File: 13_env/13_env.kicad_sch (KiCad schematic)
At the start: 51 parts, among them J1 gate in 1, J3 Eurorack, J5 env out 1, J6 End of Cycle Out, Q1 BC848, Q2 BC858, Q3 BC848, Q4 BC858, SW1 Manual Gate, SW2 Normal/Inverted, SW4 Gate/Loop, U1 TL074, U2 TL072

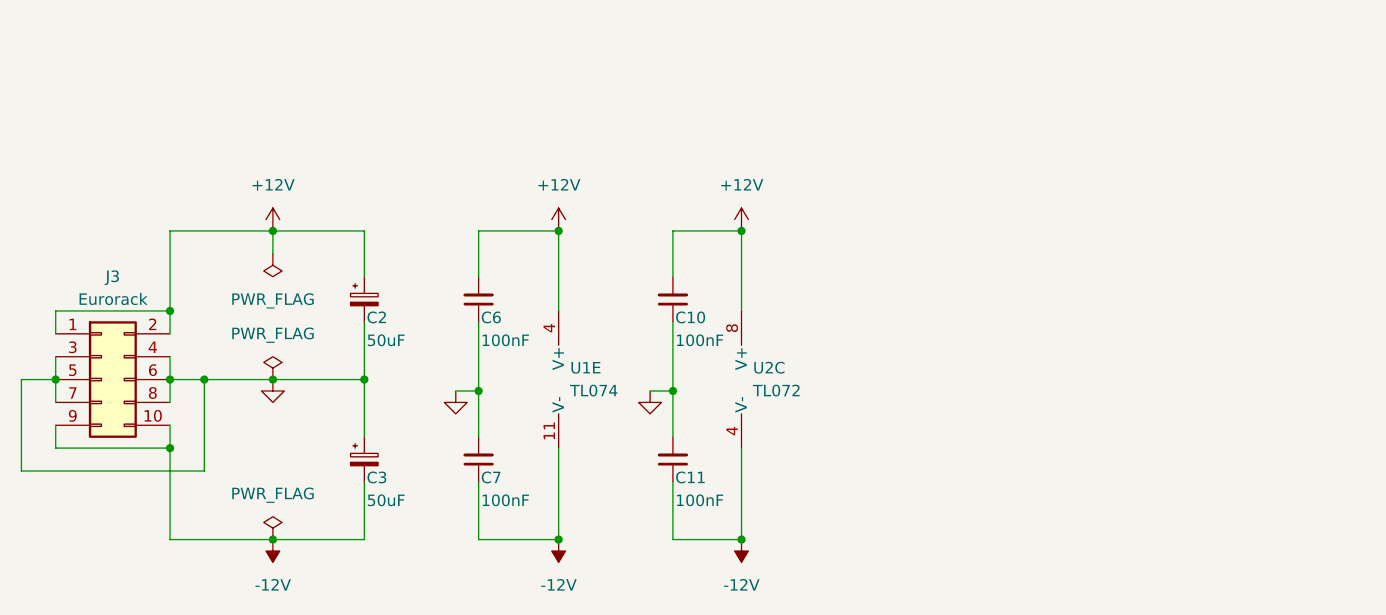
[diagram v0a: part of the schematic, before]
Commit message: added diodes
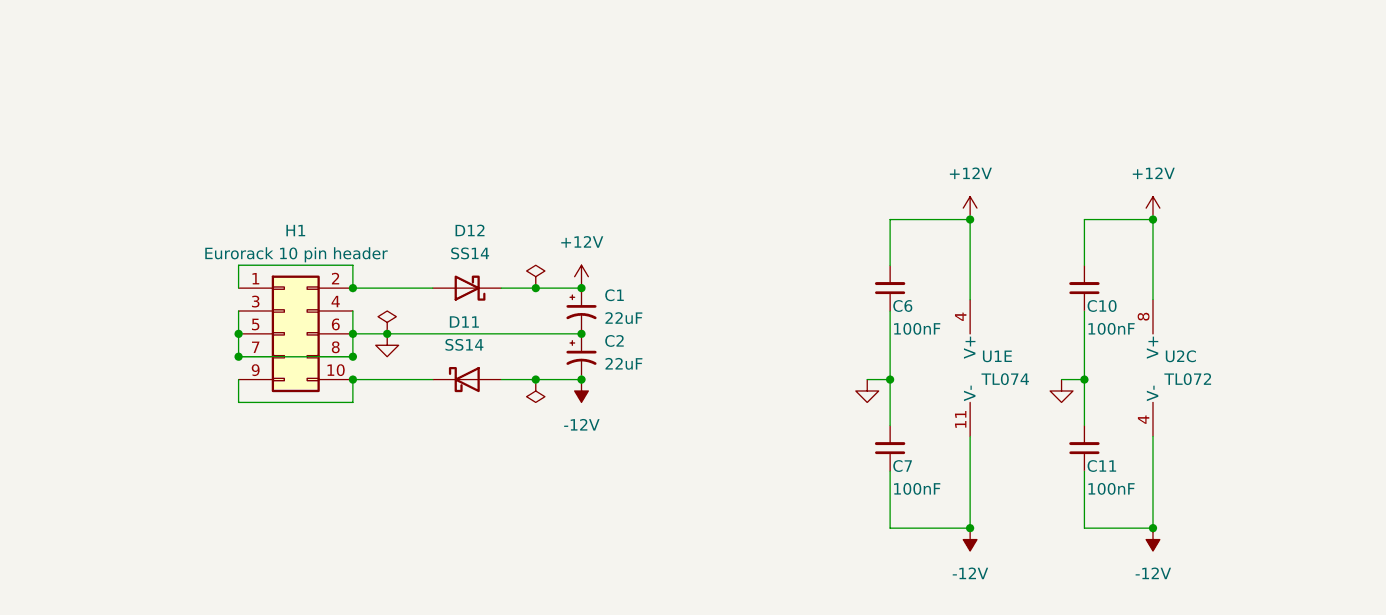
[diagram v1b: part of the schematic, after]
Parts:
- removed C2, C3: 50uF, Capacitor_THT:CP_Radial_D6.3mm_P2.50mm, symbol Device:C_Polarized_Small
- removed J3: Eurorack, cynthia:Eurorack Header, symbol Connector_Generic:Conn_02x05_Odd_Even
- added C1, C2: 22uF, Capacitor_THT:CP_Radial_D6.3mm_P2.50mm, symbol Device:C_Polarized_Small_US
- added D11, D12: SS14, Diode_SMD:D_SMA, symbol Diode:SS14
- added H1: Eurorack 10 pin header, cynthia:Eurorack Header, symbol Connector_Generic:Conn_02x05_Odd_Even
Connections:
- net +12V: now also C1.1, D12.1 (K)
- net -12V: now also C2.2, D11.2 (A)
- net GND: now also C1.2, C2.1, H1.3 (Pin_3), H1.4 (Pin_4), H1.5 (Pin_5), H1.6 (Pin_6), H1.7 (Pin_7), H1.8 (Pin_8)
- new net: D12.2 (A), H1.1 (Pin_1), H1.2 (Pin_2)
- new net: D11.1 (K), H1.10 (Pin_10), H1.9 (Pin_9)
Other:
- moved on the sheet: C10, C11, C6, C7, U1E, U2C

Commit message: updated 13 pcb
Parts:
- C10, C11, C6, C7, C8, C9: footprint Capacitor_SMD:C_0805_2012Metric_Pad1.18x1.45mm_HandSolder -> cynthia:C SMD 0805
- D1, D2, D3, D5, D6, D7: footprint Diode_SMD:D_0805_2012Metric_Pad1.15x1.40mm_HandSolder -> Diode_SMD:D_SOD-323_HandSoldering
- R15, R16, R17, R18, R19, R20, R21, R22, R23, R24, R25, R26, R27, R28, R5, R6, R7, R9: footprint Resistor_SMD:R_0805_2012Metric_Pad1.20x1.40mm_HandSolder -> cynthia:R SMD 0805
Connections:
- net at R9.1, SW2.1 (A), U2.1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: now also U1.6 (-); no longer U1.13 (-)
- net at R7.2, SW4.1 (A), U1.10 (+): now also U1.7; no longer U1.14
- net at R21.1, R26.2, R7.1: now also U1.5 (+); no longer U1.12 (+)
- net at D1.1 (K), R15.2: now also U1.12 (+); no longer U1.5 (+)
- new net: R20.1, U1.13 (-), U1.14
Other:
- moved on the sheet: C5
